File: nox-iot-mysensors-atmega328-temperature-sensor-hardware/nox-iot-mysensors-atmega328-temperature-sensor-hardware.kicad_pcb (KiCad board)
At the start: 2 copper layers, 14 parts, among them J1 Conn_01x02, J2 FTDI232, U1 ATmega328P-PU, U2 DHT11, U3 NRF24L01+, U5 LM317_3PinPackage, Y1 16 MHZ

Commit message: pcb first attemp
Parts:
- moved U2 103.5 mm to (58.1, 23.6)
- moved J2 87.7 mm to (72.9, 17.1), turned to 90 degrees
- moved Y1 82.5 mm to (78.0, 53.9), turned to 270 degrees
- moved RV1 79.6 mm to (134.5, 42.9), turned to 270 degrees
- moved R1 77.9 mm to (76.1, 46.7), turned to 90 degrees
- moved C3 77.8 mm to (81.2, 37.8), turned to 90 degrees
- moved R2 68.0 mm to (160.0, 35.0), turned to 180 degrees
- moved C2 67.2 mm to (67.2, 42.9), turned to 270 degrees
- moved C1 60.6 mm to (67.1, 62.5), turned to 90 degrees
- moved J1 47.5 mm to (134.2, 22.0)
- moved U3 23.4 mm to (140.4, 68.2), turned to 180 degrees
- moved U5 22.4 mm to (156.5, 22.8)
- moved U1 21.4 mm to (100.7, 33.2)
- moved C4 10.2 mm to (137.7, 77.2)

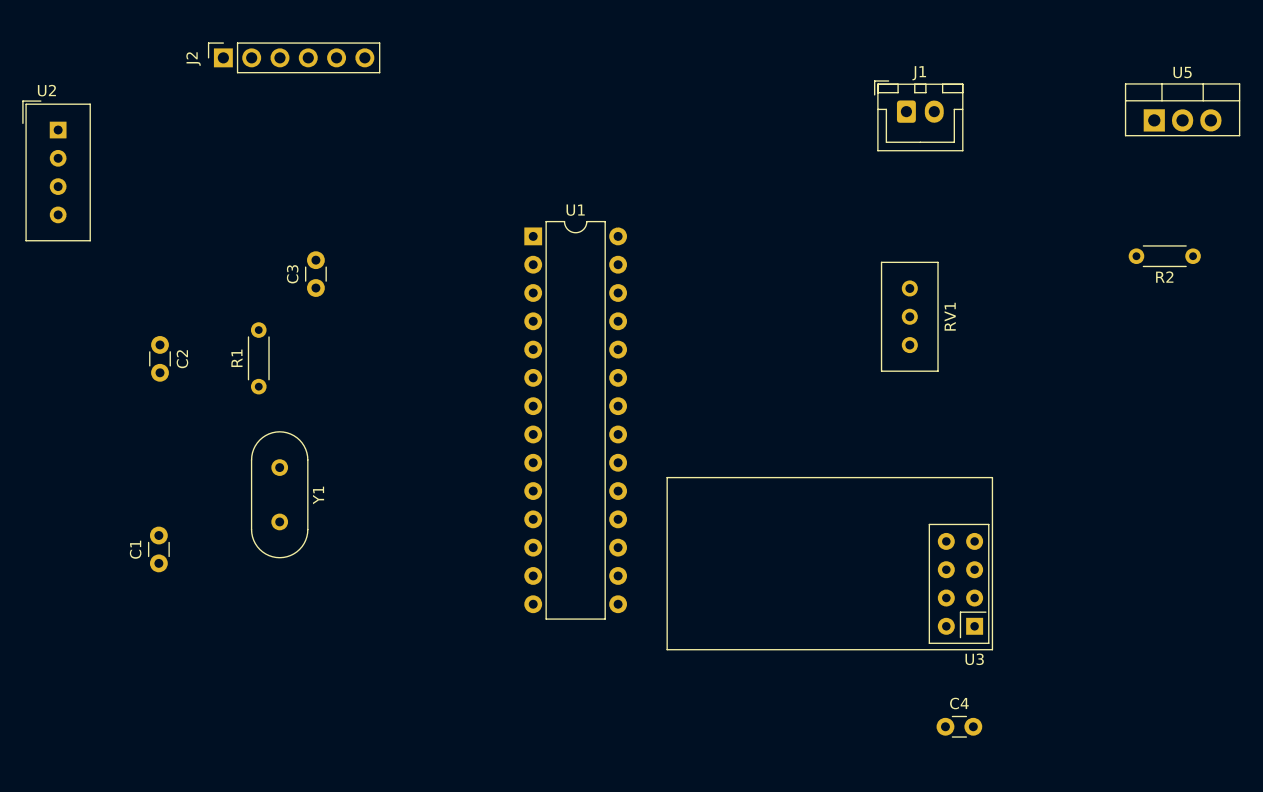
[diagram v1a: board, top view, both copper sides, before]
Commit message: aht10 sensor instead of dht11 and 3.3v boost
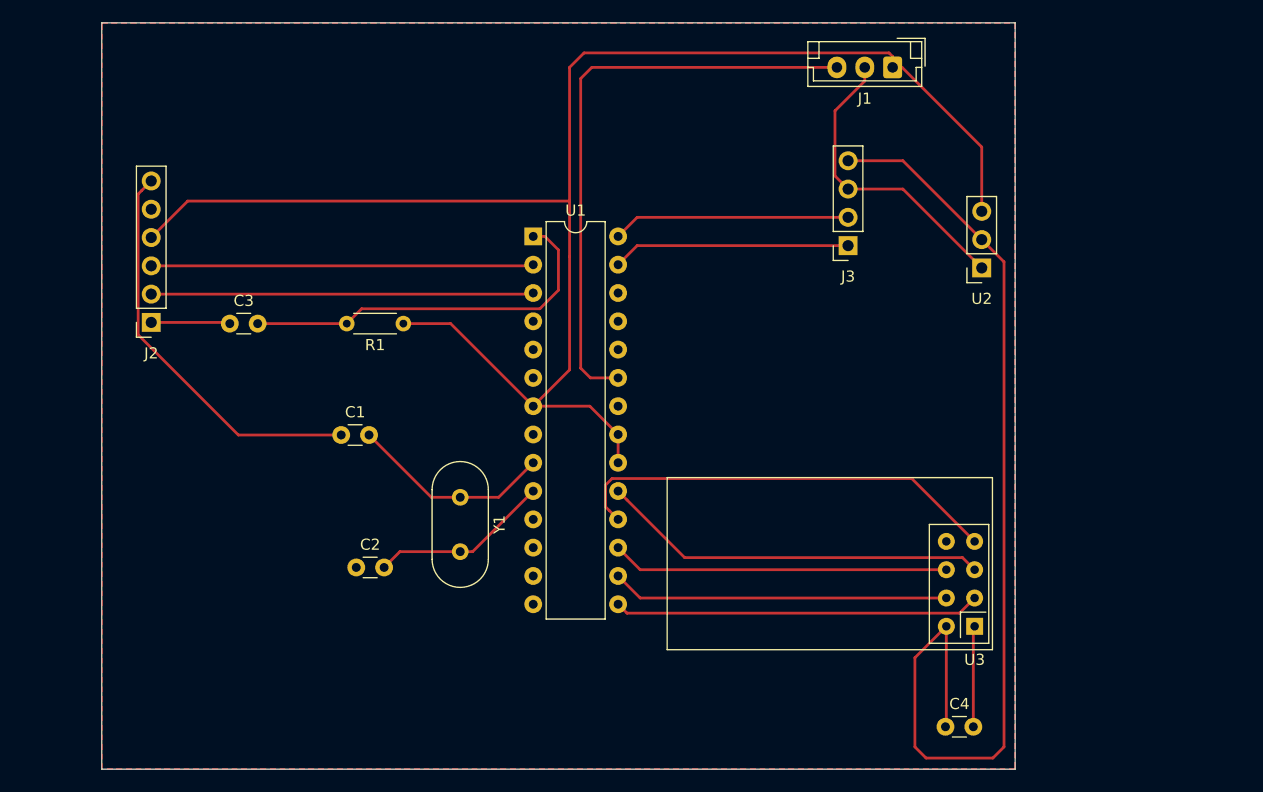
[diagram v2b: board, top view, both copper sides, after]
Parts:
- removed R2: 2K, Resistor_THT:R_Axial_DIN0204_L3.6mm_D1.6mm_P5.08mm_Horizontal
- removed RV1: 5K POT, Potentiometer_THT:Potentiometer_Bourns_3296W_Vertical
- removed U5: LM317_3PinPackage, Package_TO_SOT_THT:TO-220-3_Vertical
- added J3: AHT10, Connector_PinSocket_2.54mm:PinSocket_1x04_P2.54mm_Vertical, F.Cu at (129.0, 34.0)
- J1: value Conn_01x02 -> Conn_01x03; footprint Connector_JST:JST_XH_B2B-XH-A_1x02_P2.50mm_Vertical -> Connector_JST:JST_EH_B3B-EH-A_1x03_P2.50mm_Vertical
- U2: value DHT11 -> WAVGAT 3.3V; footprint Sensor:Aosong_DHT11_5.5x12.0_P2.54mm -> Connector_PinSocket_2.54mm:PinSocket_1x03_P2.54mm_Vertical
- moved U2 83.8 mm to (141.0, 36.0), turned to 180 degrees
- moved C2 26.6 mm to (84.9, 62.9), turned to 0 degrees
- moved J2 24.6 mm to (66.4, 40.9), turned to 180 degrees
- moved C1 20.0 mm to (83.5, 51.0), turned to 0 degrees
- moved Y1 16.4 mm to (94.2, 56.6)
- moved R1 14.2 mm to (89.1, 41.0), turned to 180 degrees
- moved C3 8.36 mm to (73.5, 41.0), turned to 0 degrees
- moved J1 4.16 mm to (133.0, 18.0), turned to 180 degrees
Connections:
- J1 pad 1: GND -> +5V
- J1 pad 2: +5V -> GND
- U1 pad 23: Net-(U1-Pad23) -> Battery+
- U1 pad 27: Net-(U1-Pad27) -> /SDA
- U1 pad 28: Net-(U1-Pad28) -> /SCL
- U2 pad 1: +5V -> GND
- U2 pad 2: Net-(U1-Pad5) -> 3.3V
- U2 pad 3: Net-(U2-Pad3) -> +5V
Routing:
- net +5V: track 0.00 -> 144.0 mm
- net 3.3V: track 0.00 -> 91.2 mm
- net GND: track 0.00 -> 72.8 mm
- net Battery+: track 0.00 -> 53.1 mm
- net Net-(U1-Pad18): track 0.00 -> 39.3 mm
- net Net-(U1-Pad19): track 0.00 -> 34.9 mm
- net Net-(C3-Pad2): track 0.00 -> 34.6 mm
- net /TX: track 0.00 -> 34.3 mm
- net /RX: track 0.00 -> 34.3 mm
- net Net-(U1-Pad15): track 0.00 -> 32.9 mm
- net Net-(U1-Pad17): track 0.00 -> 30.3 mm
- net Net-(U1-Pad16): track 0.00 -> 30.3 mm
- net /SDA: track 0.00 -> 21.4 mm
- net /SCL: track 0.00 -> 21.4 mm
- net Net-(C1-Pad2): track 0.00 -> 18.3 mm
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- added copper zone on F.Cu, net GND
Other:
- board outline added: 82 x 67 mm

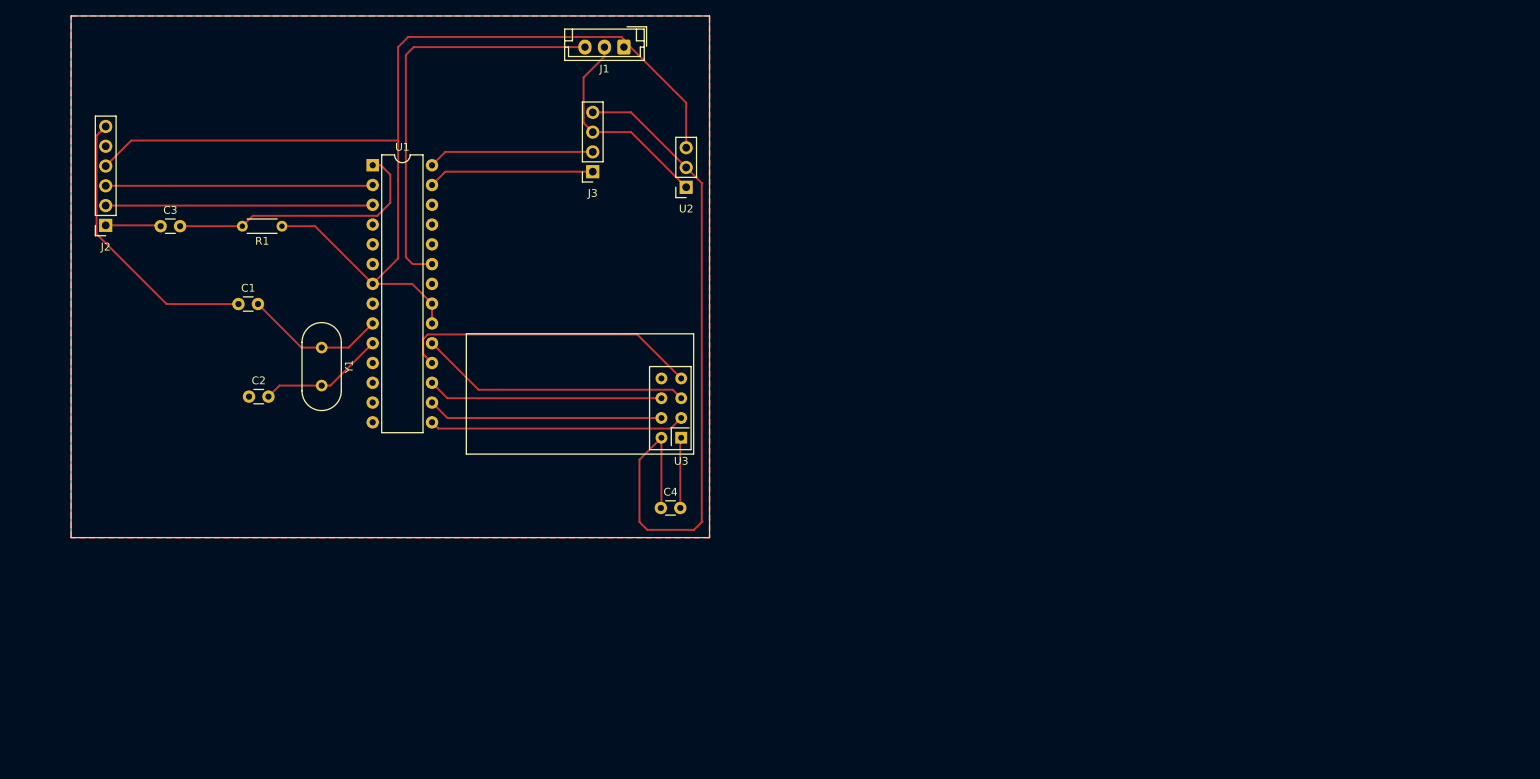
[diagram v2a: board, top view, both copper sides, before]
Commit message: components in place
before wiring components por perfboard
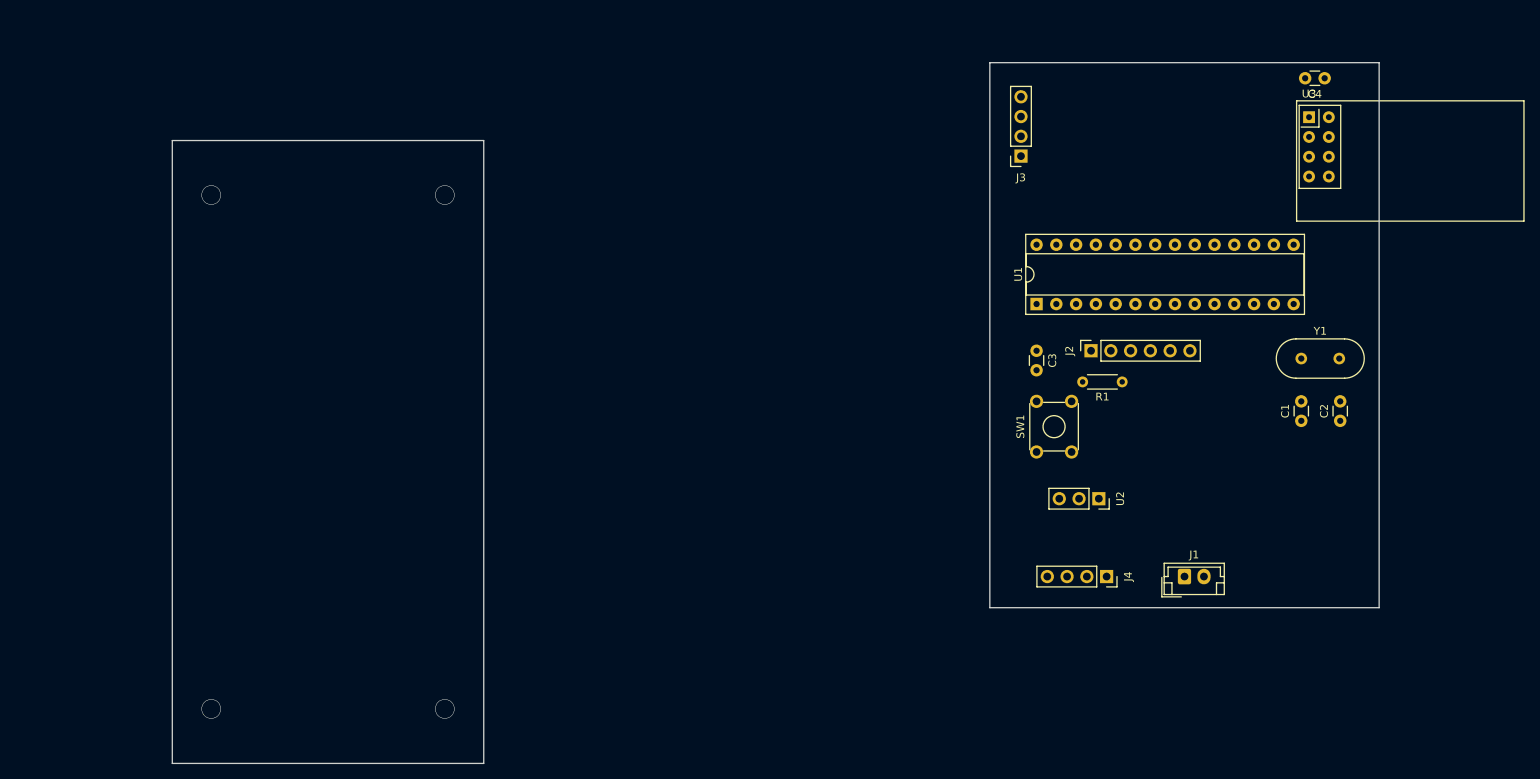
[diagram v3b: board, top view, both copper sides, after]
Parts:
- added J4: TP4056, Connector_PinSocket_2.54mm:PinSocket_1x04_P2.54mm_Vertical, F.Cu at (195.0, 86.0)
- added SW1: Reset, Button_Switch_THT:SW_TH_Tactile_Omron_B3F-10xx, F.Cu at (186.0, 70.0)
- J1: value Conn_01x03 -> Vin; footprint Connector_JST:JST_EH_B3B-EH-A_1x03_P2.50mm_Vertical -> Connector_JST:JST_EH_B2B-EH-A_1x02_P2.50mm_Vertical
- U1: footprint Package_DIP:DIP-28_W7.62mm -> Package_DIP:DIP-28_W7.62mm_Socket
- moved C2 140.2 mm to (225.0, 66.0), turned to 90 degrees
- moved C1 137.3 mm to (220.0, 66.0), turned to 90 degrees
- moved J2 127.6 mm to (193.0, 57.0), turned to 90 degrees
- moved Y1 125.8 mm to (220.0, 58.0), turned to 0 degrees
- moved C3 113.6 mm to (186.0, 57.0), turned to 270 degrees
- moved R1 109.8 mm to (197.0, 61.0)
- moved C4 101.6 mm to (223.0, 22.0), turned to 180 degrees
- moved J1 99.0 mm to (205.0, 86.0), turned to 0 degrees
- moved U3 90.5 mm to (221.0, 27.0), turned to 0 degrees
- moved U1 87.1 mm to (186.0, 51.0), turned to 90 degrees
- moved U2 66.4 mm to (194.0, 76.0), turned to 270 degrees
- moved J3 55.0 mm to (184.0, 32.0)
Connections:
- J1 pad 1: +5V -> +BATT
- J1 pad 2: GND -> -BATT
- J2 pad 4: +5V -> 3.3V
- R1 pad 1: +5V -> 3.3V
- U1 pad 20: +5V -> 3.3V
- U1 pad 21: +5V -> Net-(U1-Pad21)
- U1 pad 23: Battery+ -> Net-(U1-Pad23)
- U1 pad 7: +5V -> 3.3V
- U2 pad 3: +5V -> +4V
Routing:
- net +5V: track 144.0 -> 0.00 mm
- net 3.3V: track 91.2 -> 0.00 mm
- net GND: track 72.8 -> 0.00 mm
- net Battery+: track 53.1 -> 0.00 mm
- net Net-(U1-Pad18): track 39.3 -> 0.00 mm
- net Net-(U1-Pad19): track 34.9 -> 0.00 mm
- net Net-(C3-Pad2): track 34.6 -> 0.00 mm
- net /TX: track 34.3 -> 0.00 mm
- net /RX: track 34.3 -> 0.00 mm
- net Net-(U1-Pad15): track 32.9 -> 0.00 mm
- net Net-(U1-Pad17): track 30.3 -> 0.00 mm
- net Net-(U1-Pad16): track 30.3 -> 0.00 mm
- net /SDA: track 21.4 -> 0.00 mm
- net /SCL: track 21.4 -> 0.00 mm
- net Net-(C1-Pad2): track 18.3 -> 0.00 mm
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- removed copper zone on F.Cu, net GND
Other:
- board size 82 x 67 mm -> 155 x 90 mm

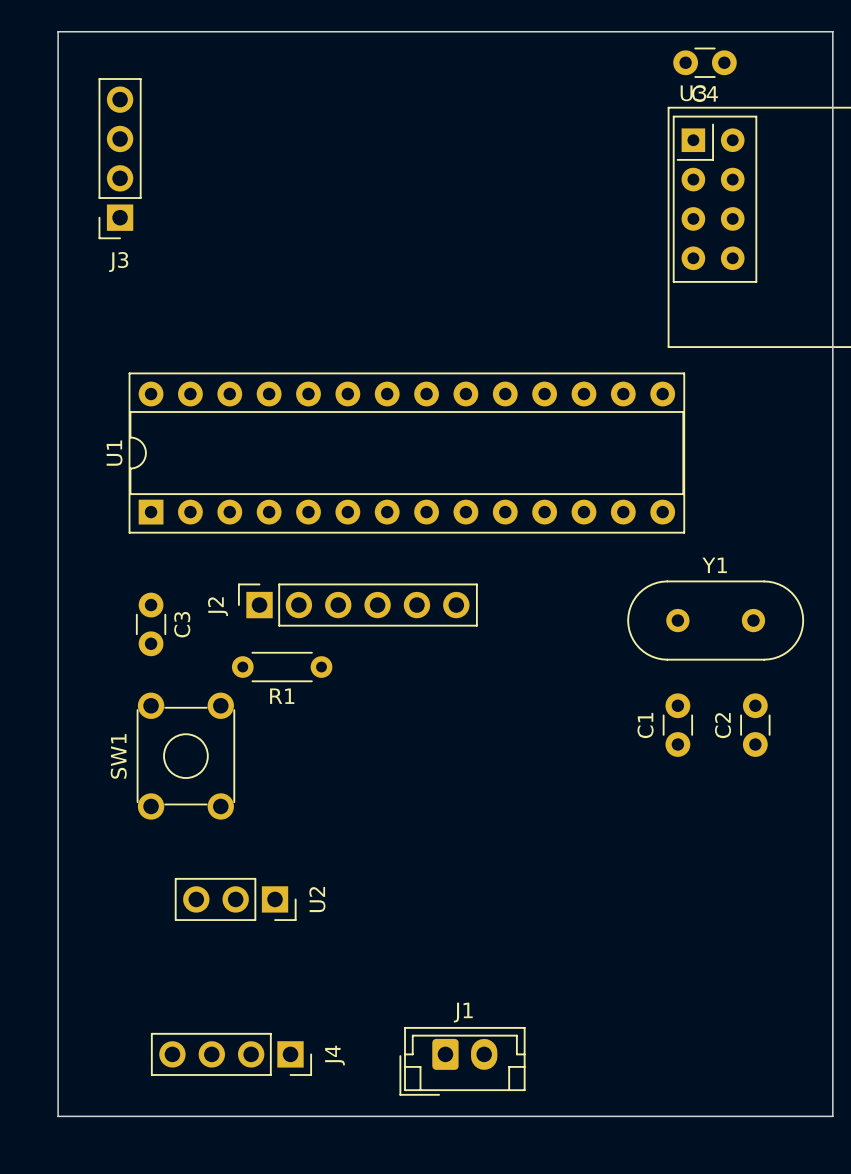
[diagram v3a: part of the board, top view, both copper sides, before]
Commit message: wires complete for perfboard
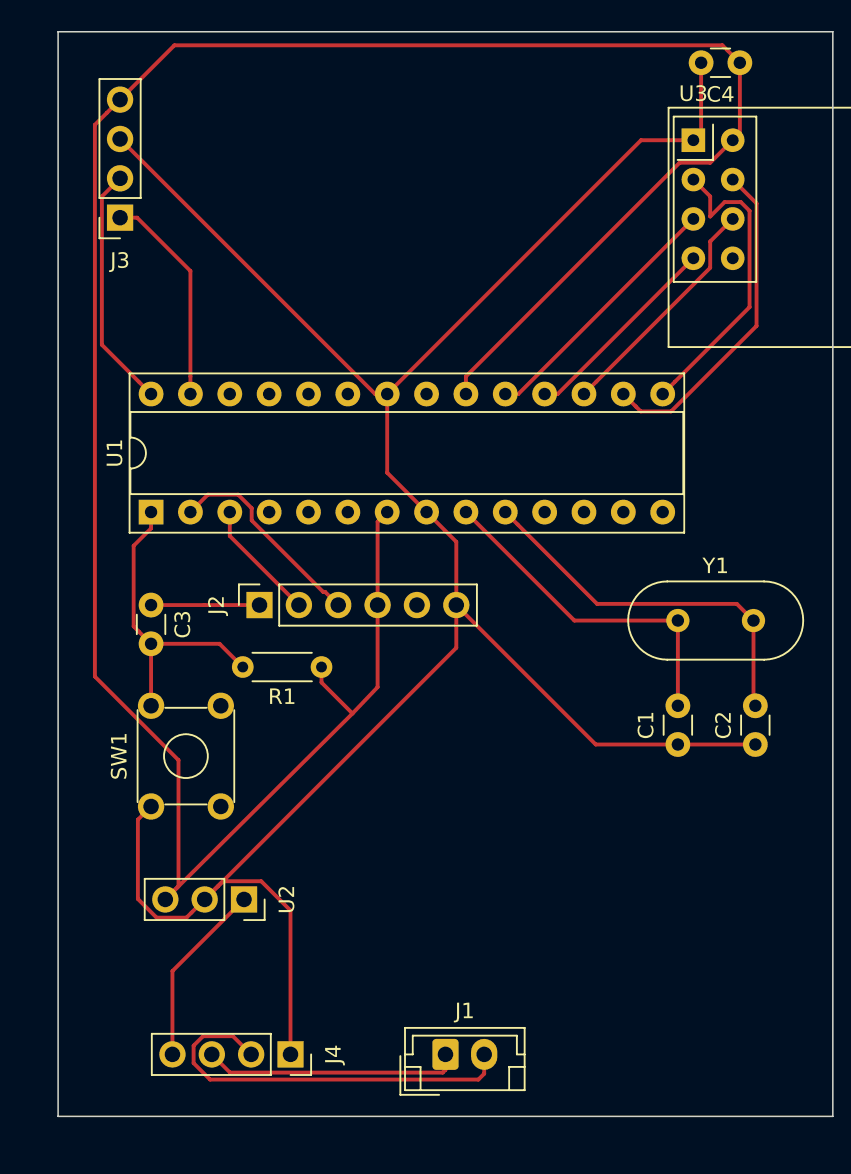
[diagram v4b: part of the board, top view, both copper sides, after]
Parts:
- moved U2 2.00 mm to (192.0, 76.0)
- moved C4 1.00 mm to (224.0, 22.0)
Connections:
- U2 pad 1: GND -> +4V
- U2 pad 2: 3.3V -> GND
- U2 pad 3: +4V -> 3.3V
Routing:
- net 3.3V: track 0.00 -> 161.4 mm
- net GND: track 0.00 -> 147.7 mm
- net -BATT: track 0.00 -> 26.2 mm
- net Net-(C2-Pad2): track 0.00 -> 24.5 mm
- net Net-(C1-Pad2): track 0.00 -> 22.1 mm
- net Net-(U1-Pad16): track 0.00 -> 21.4 mm
- net Net-(U1-Pad15): track 0.00 -> 20.1 mm
- net Net-(C3-Pad2): track 0.00 -> 20.0 mm
- net Net-(U1-Pad19): track 0.00 -> 16.8 mm
- net +BATT: track 0.00 -> 16.6 mm
- net /SCL: track 0.00 -> 15.7 mm
- net Net-(U1-Pad17): track 0.00 -> 15.3 mm
- net /SDA: track 0.00 -> 13.9 mm
- net /TX: track 0.00 -> 13.4 mm
- net Net-(U1-Pad18): track 0.00 -> 13.2 mm
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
